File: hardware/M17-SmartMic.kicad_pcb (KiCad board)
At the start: 4 copper layers, 99.5 x 80 mm, 205 parts, among them IC301 LM4991MA, J301 CAT_TX, J302 CAT_RX, J401 Radio, J402 USB_C, J403 Radio_Opt, J404 Kenwood-3.5, J405 Kenwood-2.5, J406 OLED, J407 KH-RJ45-58-8P8C, J408 STLink, J409 UART, J410 Speaker, J411 +12V, J412 Hirose FH12-26S-0.5SH(55), J413 Molex 532610271, Q201 MMBT3904, Q202 IRLML2244, Q301 IRLML2060, Q302 BSS138, Q303 BSS138, SW201 Button Power, SW202 Reset, SW203 Button Enter, SW204 Button Left, SW205 Button Up, SW206 Button Down, SW207 Button Escape, SW208 Button Right, U201 STM32F405RGTx, U202 TPS7A2033, U203 TP6841S6, U301 MCP6002, U302 MAX9814, U401 USBLC6-2SC6, U501 MCP4551-103, U502 MCP4551-103, U503 MCP6002, U504 MCP6002, Y201 8 MHz

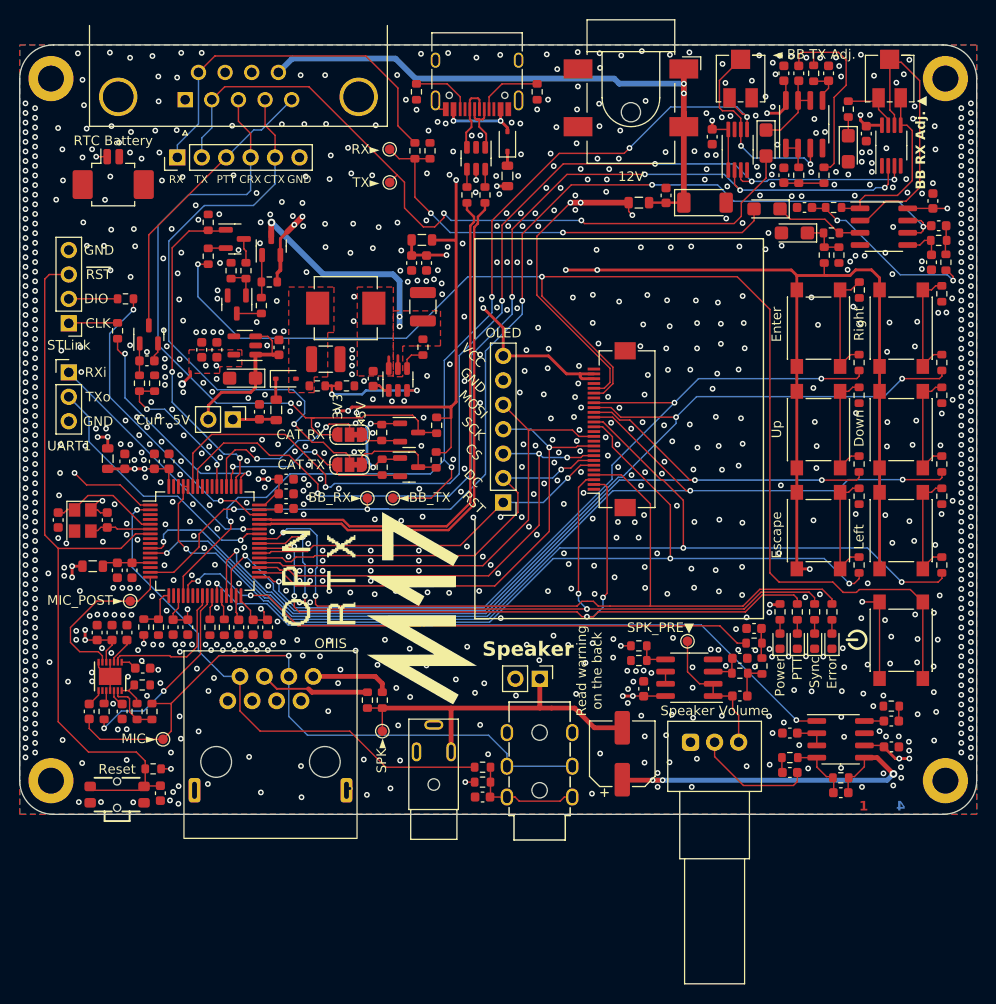
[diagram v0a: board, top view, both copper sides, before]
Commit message: Updated power supply low pass filter
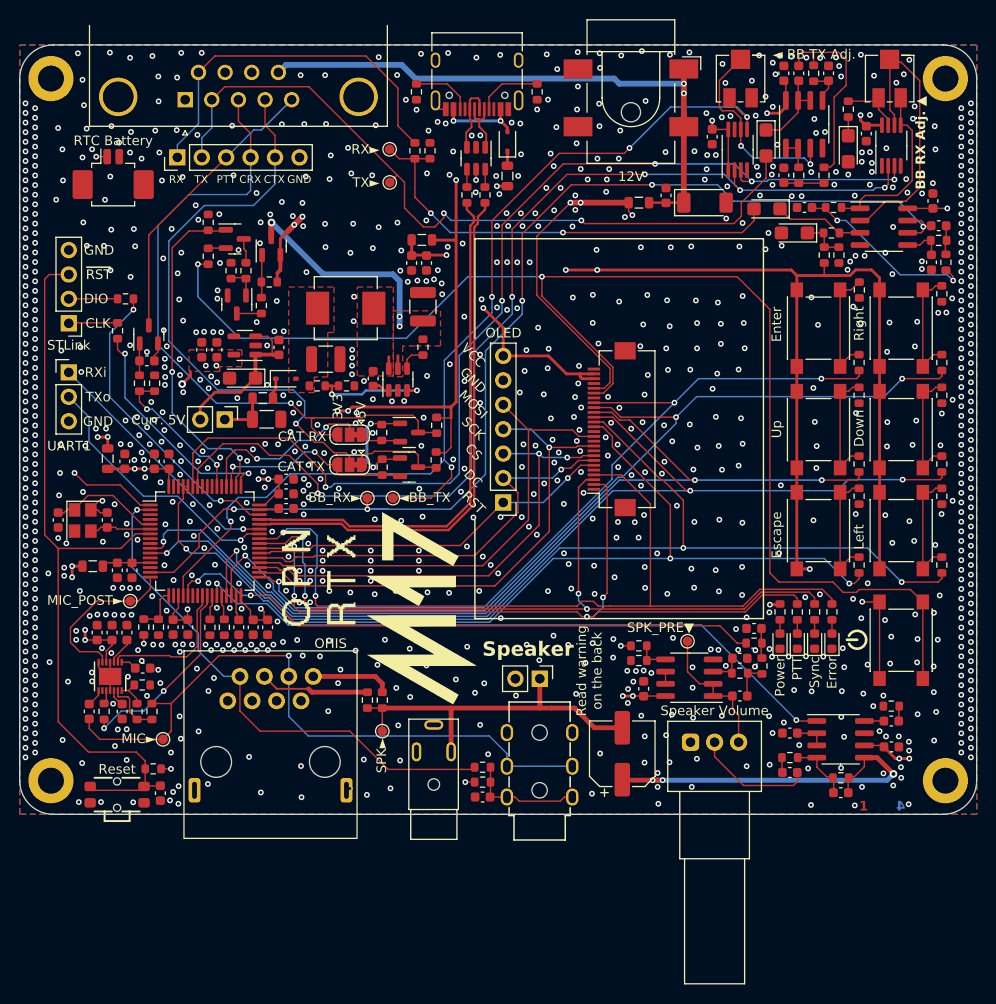
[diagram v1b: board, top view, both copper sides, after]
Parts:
- C223: footprint Capacitor_SMD:C_0603_1608Metric -> Capacitor_SMD:C_1206_3216Metric
- L202: value 5u -> 1u
- moved L202 1.86 mm to (195.5, 85.2), turned to 0 degrees
- moved C223 1.08 mm to (195.9, 87.4), turned to 0 degrees
- moved JP201 0.84 mm to (191.6, 87.5)
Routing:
- net GPIO_POWER: track 34.6 -> 35.3 mm
- net +5V: track 236.5 -> 237.1 mm
- net Net-(JP201-A): track 4.53 -> 5.12 mm
- net LINE: track 63.8 -> 63.3 mm
- net GND: vias 1038 -> 1052

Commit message: Updated various symbols attributes
Updated various components (mostly LEDs and switches) to simplify the BOM and make it more easily readable.
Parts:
- D201: value DFLT18A-7 -> PTVS18VP1UP
- D204: value Power -> Blue
- D205: value PTT -> Red
- D206: value Sync -> Green
- D207: value Error -> Orange
- J406: value OLED -> 2.54mm Header 7p
- R202: value 10kR -> 10k
- SW201: value Button Power -> Tactile switch
- SW202: value Reset -> Tactile switch
- SW203: value Button Enter -> Tactile switch
- SW204: value Button Left -> Tactile switch
- SW205: value Button Up -> Tactile switch
- SW206: value Button Down -> Tactile switch
- SW207: value Button Escape -> Tactile switch
- SW208: value Button Right -> Tactile switch

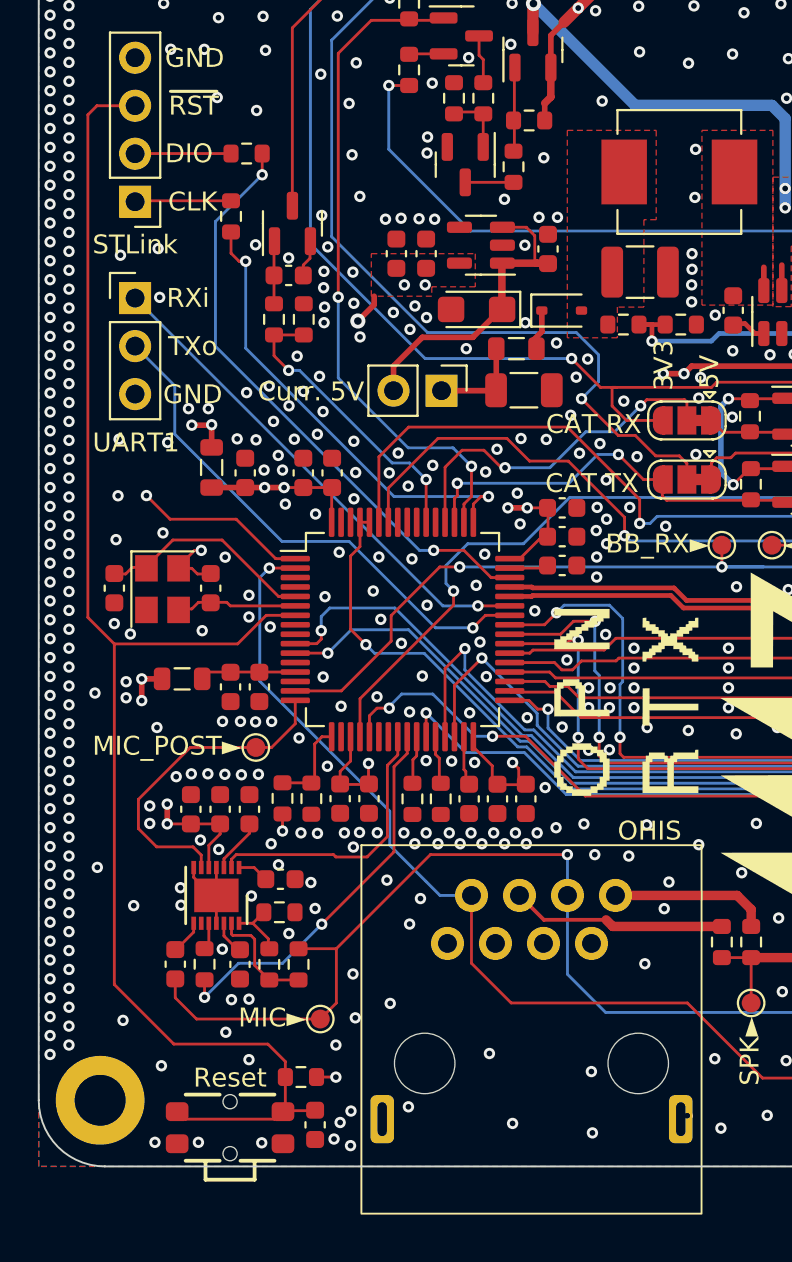
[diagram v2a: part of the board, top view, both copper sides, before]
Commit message: Updated DC-DC output capacitor
Using 1206 footprint
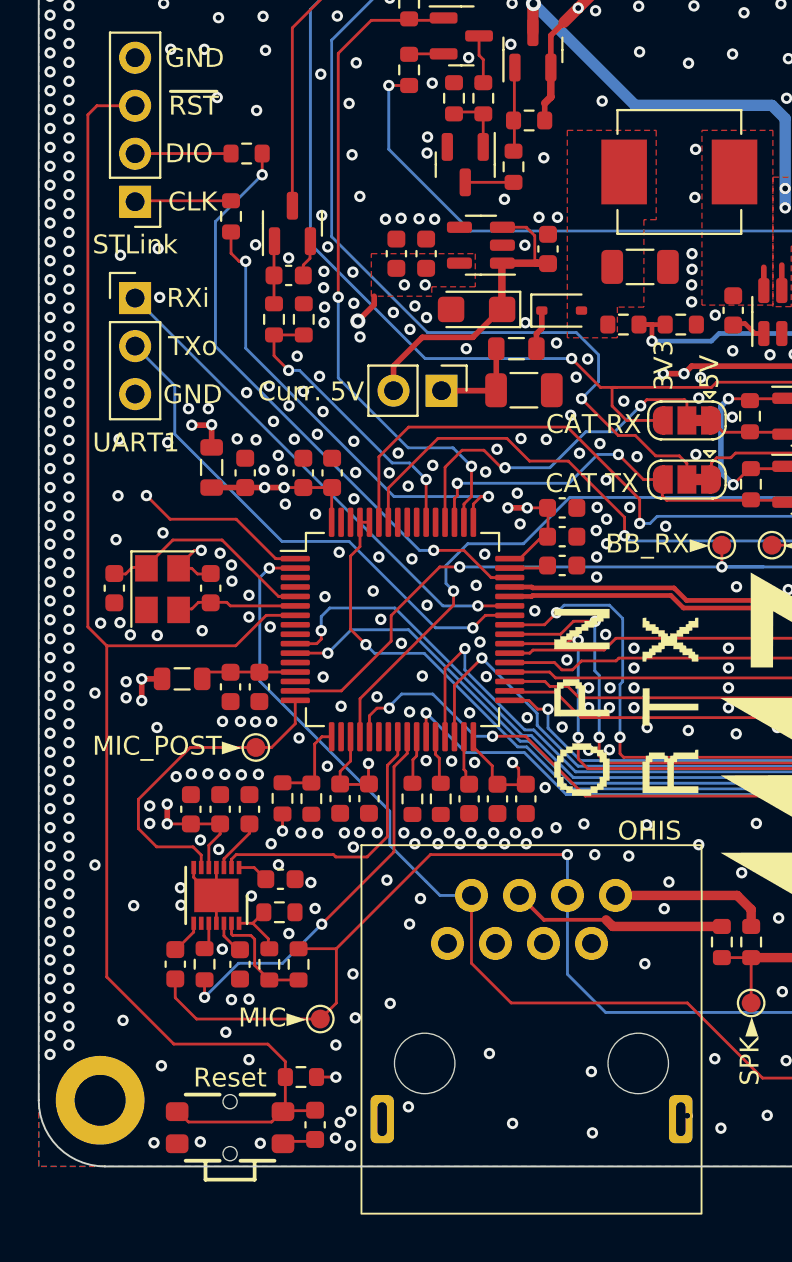
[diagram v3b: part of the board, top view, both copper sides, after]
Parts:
- C212: footprint Capacitor_SMD:C_1210_3225Metric -> Capacitor_SMD:C_1206_3216Metric
- moved C212 0.27 mm to (202.1, 80.9)
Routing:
- net GND: track 11.9 -> 13.7 mm, vias 1052 -> 1056
- net NRST: track 80.6 -> 81.1 mm
